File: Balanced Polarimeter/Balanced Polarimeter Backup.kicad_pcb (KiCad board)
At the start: 2 copper layers, 52 x 46 mm, 15 parts, among them IC1 OP27, Q1 MMPQ3904, Q2 MMPQ3904, U1 ADA4898-1YRDZ, U2 ADA4898-1YRDZ

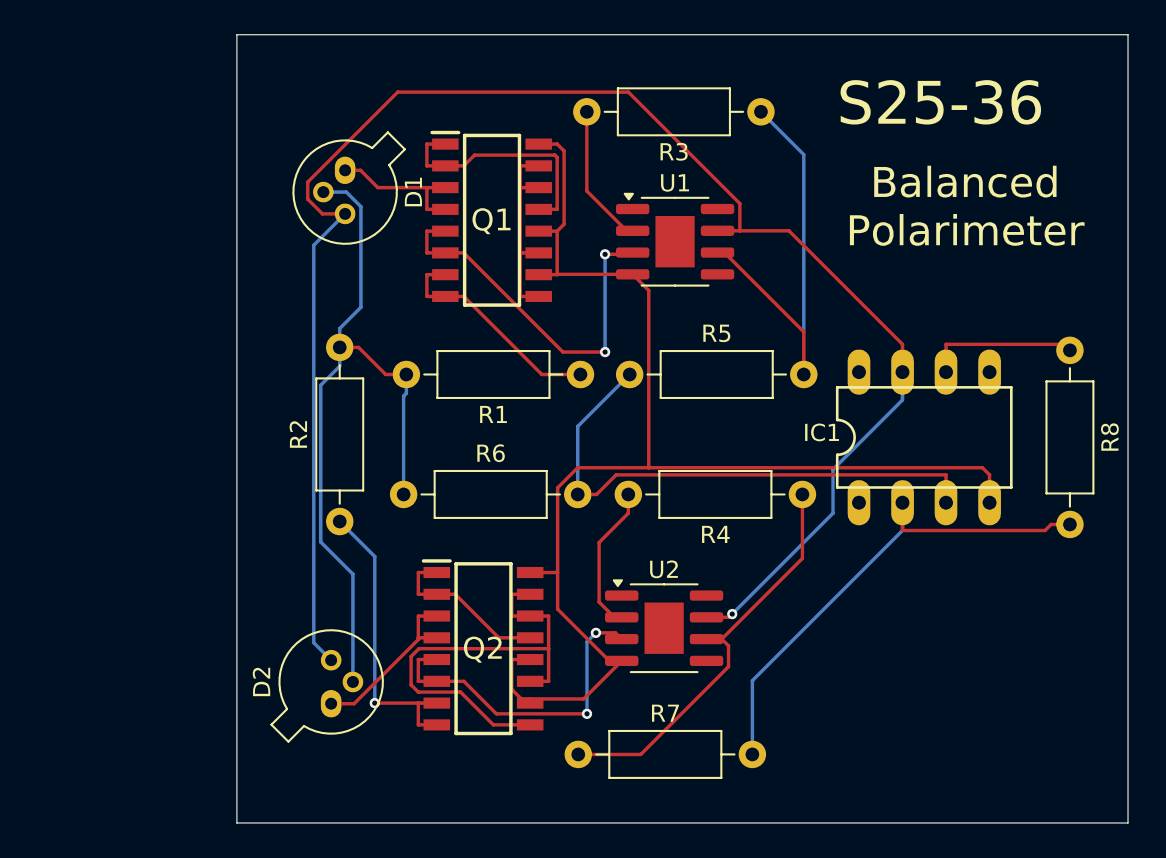
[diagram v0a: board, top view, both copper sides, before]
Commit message: PCB Start Design
Edited the naming of some components and created a PCB to layout. It's still missing the BNC connector for now
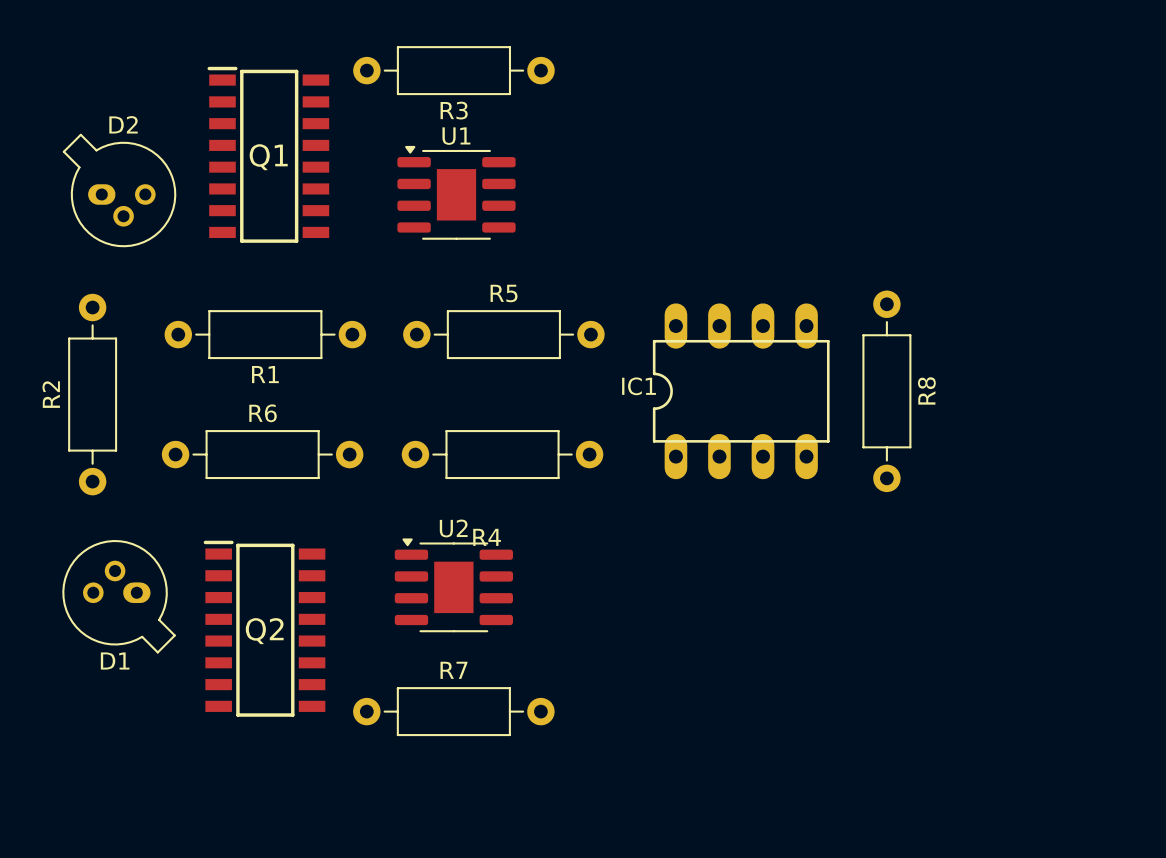
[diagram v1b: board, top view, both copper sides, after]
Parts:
- moved R2 14.6 mm to (118.6, 85.6)
- moved D2 14.3 mm to (119.1, 68.8), turned to 0 degrees
- moved Q1 13.5 mm to (128.9, 66.6)
- moved R6 13.5 mm to (123.4, 84.0)
- moved R1 13.5 mm to (133.7, 77.0)
- moved R3 13.1 mm to (144.7, 61.6)
- moved D1 13.1 mm to (121.2, 92.1), turned to 180 degrees
- moved U1 13.0 mm to (139.8, 68.8)
- moved Q2 12.8 mm to (128.7, 94.2)
- moved R4 12.6 mm to (147.6, 84.0)
- moved R5 12.6 mm to (137.5, 77.0)
- moved R7 12.6 mm to (134.6, 99.0)
- moved U2 12.5 mm to (139.7, 91.8)
- moved IC1 11.0 mm to (156.4, 80.3)
- moved R8 11.0 mm to (164.9, 75.2)
- renumbered D2 to D1, D1 to D2
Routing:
- net +5V: track 97.4 -> 0.00 mm, vias 1 -> 0
- net -5V: track 79.0 -> 0.00 mm
- net GND: track 43.6 -> 0.00 mm
- net Net-(IC1-Pad3): track 31.8 -> 0.00 mm
- net Net-(IC1-Pad2): track 29.9 -> 0.00 mm
- net Net-(Q2-BASE_#1): track 27.2 -> 0.00 mm
- net Net-(R3-Pad1): track 25.8 -> 0.00 mm
- net Net-(R4-Pad1): track 23.9 -> 0.00 mm
- net Net-(Q1-COLLECTOR_#3_1): track 22.5 -> 0.00 mm, vias 2 -> 0
- net Net-(Q2-COLLECTOR_#3_1): track 19.6 -> 0.00 mm, vias 2 -> 0
- net Net-(Q2-COLLECTOR_#4_1): track 17.4 -> 0.00 mm, vias 1 -> 0
- net Net-(Q1-BASE_#2): track 14.4 -> 0.00 mm
- net Net-(Q1-COLLECTOR_#4_1): track 13.2 -> 0.00 mm
- net Net-(Q1-BASE_#1): track 11.9 -> 0.00 mm
- net Net-(D1-K): track 10.2 -> 0.00 mm
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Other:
- board outline removed
- board text removed: "Balanced Polarimeter"
- board text removed: "S25-36"
